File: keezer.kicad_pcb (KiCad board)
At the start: 2 copper layers, 48 parts, among them J1 Barrel_Jack, J10 REF, J11 Display, J12 Mode Switch, J13 Tare Switch, J14 Rocker Switch, J15 Conn_01x03_Male, J16 Conn_01x03_Male, J2 Relay, J3 Fan, J4 Conn_01x03_Female, J5 Conn_01x03_Female, J6 Conn_01x04_Female, J7 Conn_01x04_Female, J8 Conn_01x04_Female, J9 Conn_01x04_Female, Q1 2N5194, U1 4N25, U2 INA828, U3 INA828, U4 INA828, U5 INA828

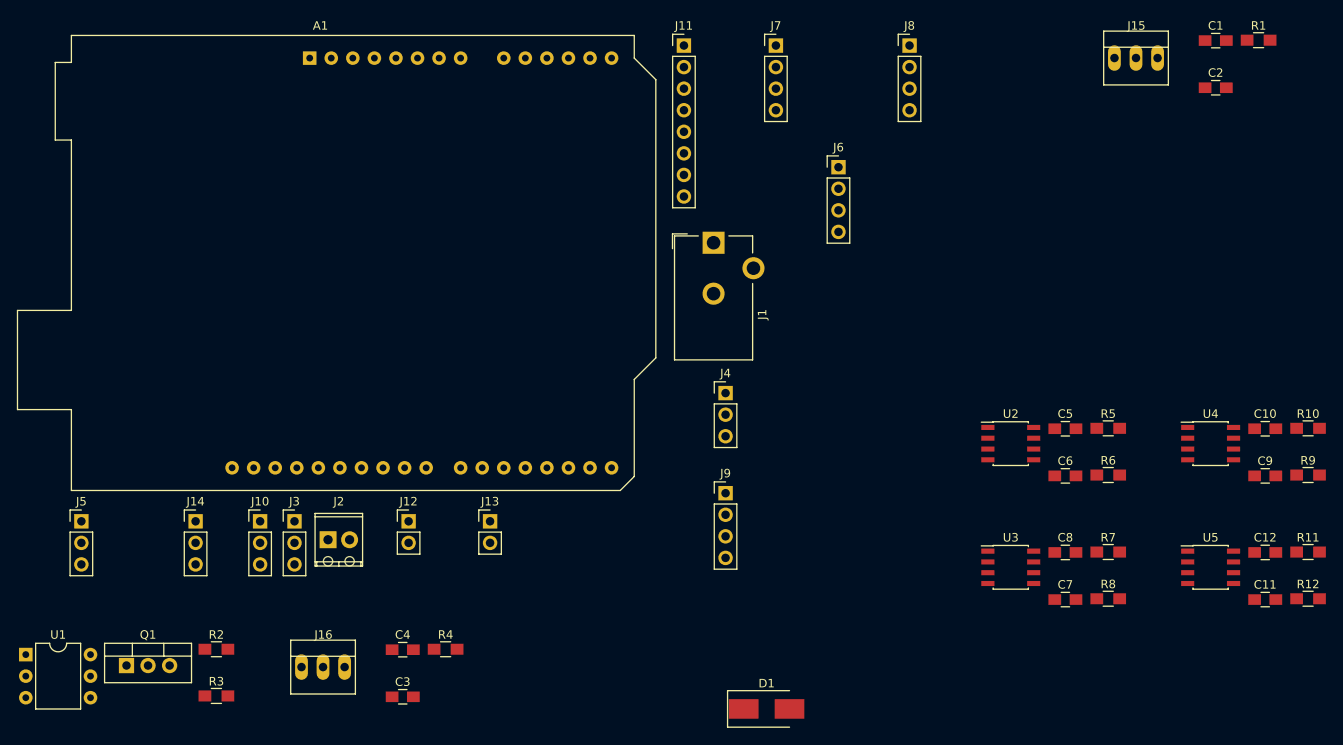
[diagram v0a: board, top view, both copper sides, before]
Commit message: Pretty much ready to go. Should verify barrel jack first. Needs a logo.
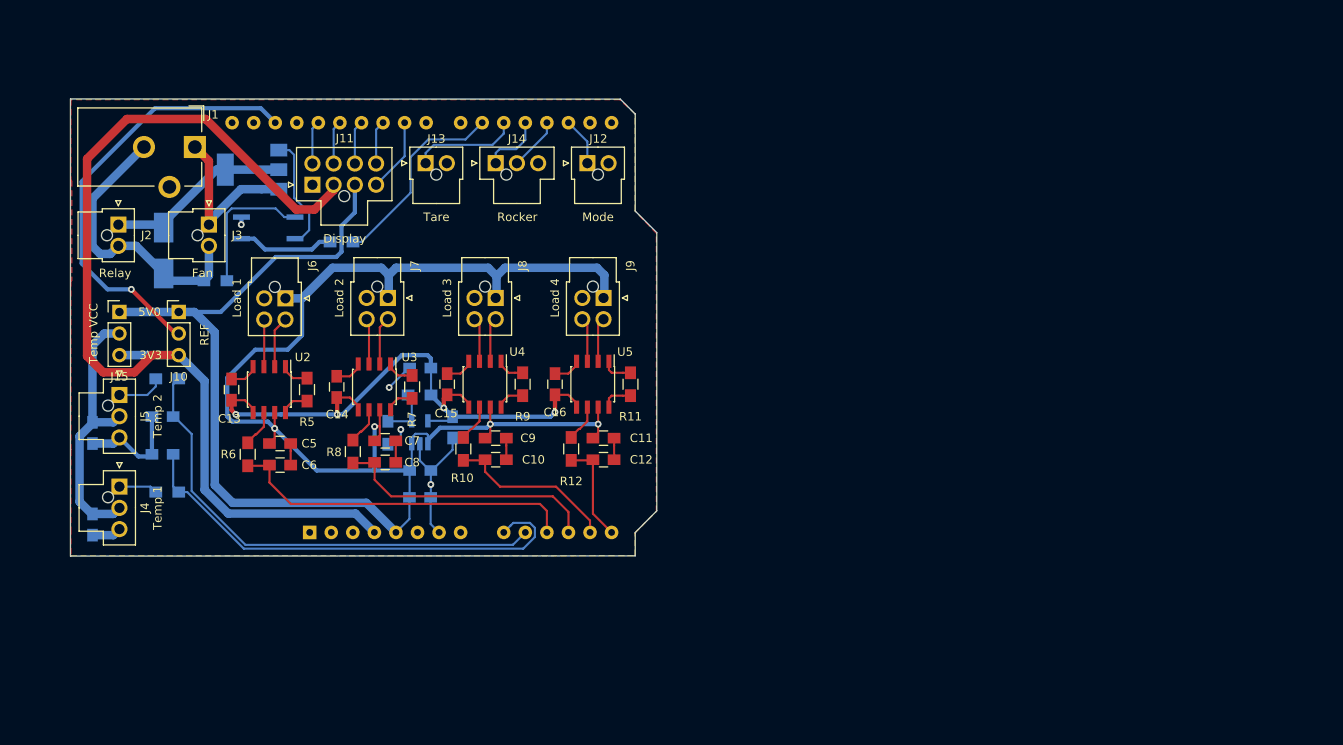
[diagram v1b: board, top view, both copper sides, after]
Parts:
- removed J16: Conn_01x03_Male, Connectors:PINHEAD1-3
- added C13: 1uF, Capacitors_SMD:C_0805_HandSoldering, F.Cu at (100.3, 92.1)
- added C14: 1uF, Capacitors_SMD:C_0805_HandSoldering, F.Cu at (112.7, 91.8)
- added C15: 1uF, Capacitors_SMD:C_0805_HandSoldering, F.Cu at (125.7, 91.4)
- added C16: 1uF, Capacitors_SMD:C_0805_HandSoldering, F.Cu at (138.4, 91.4)
- added C17: 10uF, Capacitors_SMD:C_0805_HandSoldering, B.Cu at (122.5, 104.8)
- added C18: 0.1uF, Capacitors_SMD:C_0805_HandSoldering, B.Cu at (122.6, 101.6)
- added C19: 0.1uF, Capacitors_SMD:C_0805_HandSoldering, B.Cu at (126.4, 96.5)
- added C20: 10uF, Capacitors_SMD:C_0805_HandSoldering, B.Cu at (122.6, 89.5)
- added R13: DNP, Resistors_SMD:R_0805_HandSoldering, B.Cu at (122.5, 92.7)
- added R14: DNP, Resistors_SMD:R_0805_HandSoldering, B.Cu at (118.7, 97.2)
- added U6: LDK320M18R, TO_SOT_Packages_SMD:SOT-23-5_HandSoldering, B.Cu at (122.5, 97.1)
- A1, C1, C2, C3, C4, D1, R1, R2, R3, R4: moved to B.Cu
- J11: footprint Pin_Headers:Pin_Header_Straight_1x08_Pitch2.54mm -> Connectors_Molex:Molex_NanoFit_2x04x2.50mm_Straight
- J12: value Mode Switch -> Mode; footprint Pin_Headers:Pin_Header_Straight_1x02_Pitch2.54mm -> Connectors_Molex:Molex_NanoFit_1x02x2.50mm_Straight
- J13: value Tare Switch -> Tare; footprint Pin_Headers:Pin_Header_Straight_1x02_Pitch2.54mm -> Connectors_Molex:Molex_NanoFit_1x02x2.50mm_Straight
- J14: value Rocker Switch -> Rocker; footprint Pin_Headers:Pin_Header_Straight_1x03_Pitch2.54mm -> Connectors_Molex:Molex_NanoFit_1x03x2.50mm_Straight
- J15: value Conn_01x03_Male -> Temp VCC; footprint Connectors:PINHEAD1-3 -> Pin_Headers:Pin_Header_Straight_1x03_Pitch2.54mm
- J2: footprint TerminalBlock_Phoenix:TerminalBlock_Phoenix_MPT-2.54mm_2pol -> Connectors_Molex:Molex_NanoFit_1x02x2.50mm_Straight
- J3: footprint Pin_Headers:Pin_Header_Straight_1x03_Pitch2.54mm -> Connectors_Molex:Molex_NanoFit_1x02x2.50mm_Straight
- J4: value Conn_01x03_Female -> Temp 1; footprint Pin_Headers:Pin_Header_Straight_1x03_Pitch2.54mm -> Connectors_Molex:Molex_NanoFit_1x03x2.50mm_Straight
- J5: value Conn_01x03_Female -> Temp 2; footprint Pin_Headers:Pin_Header_Straight_1x03_Pitch2.54mm -> Connectors_Molex:Molex_NanoFit_1x03x2.50mm_Straight
- J6: value Conn_01x04_Female -> Load 1; footprint Pin_Headers:Pin_Header_Straight_1x04_Pitch2.54mm -> Connectors_Molex:Molex_NanoFit_2x02x2.50mm_Straight
- J7: value Conn_01x04_Female -> Load 2; footprint Pin_Headers:Pin_Header_Straight_1x04_Pitch2.54mm -> Connectors_Molex:Molex_NanoFit_2x02x2.50mm_Straight
- J8: value Conn_01x04_Female -> Load 3; footprint Pin_Headers:Pin_Header_Straight_1x04_Pitch2.54mm -> Connectors_Molex:Molex_NanoFit_2x02x2.50mm_Straight
- J9: value Conn_01x04_Female -> Load 4; footprint Pin_Headers:Pin_Header_Straight_1x04_Pitch2.54mm -> Connectors_Molex:Molex_NanoFit_2x02x2.50mm_Straight
- Q1: value 2N5194 -> BCP51; footprint TO_SOT_Packages_THT:TO-220-3_Vertical -> TO_SOT_Packages_SMD:SOT-223-3_TabPin2; moved to B.Cu
- R11, R5, R7, R9: value 49.9 -> 75.0
- U1: value 4N25 -> FOD817D3SD; footprint Housings_DIP:DIP-6_W7.62mm -> Housings_SOIC:SO-4_4.4x3.6mm_Pitch2.54mm; moved to B.Cu
- moved C1 140.1 mm to (83.9, 97.2), turned to 270 degrees
- moved R1 134.6 mm to (92.8, 90.8), turned to 180 degrees
- moved C2 130.0 mm to (92.2, 95.2), turned to 180 degrees
- moved J15 121.0 mm to (87.1, 82.9)
- moved R6 101.4 mm to (102.2, 99.7), turned to 90 degrees
- moved R10 99.5 mm to (127.6, 99.1), turned to 90 degrees
- moved R5 94.5 mm to (109.2, 92.1), turned to 270 degrees
- moved R9 93.1 mm to (134.6, 91.4), turned to 270 degrees
- moved C5 92.5 mm to (106.0, 98.4)
- moved C6 92.5 mm to (106.0, 101.0)
- moved C9 90.7 mm to (131.4, 97.8)
- moved C10 90.7 mm to (131.4, 100.3)
- moved R8 90.6 mm to (114.6, 99.4), turned to 90 degrees
- moved D1 89.2 mm to (92.3, 75.7), turned to 270 degrees
- moved R12 88.6 mm to (140.3, 99.1), turned to 90 degrees
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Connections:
- A1 pad 20: Net-(A1-Pad18) -> Net-(A1-Pad20)
- C3 pad 1: /sheet5A46696F/Power -> /Temp Sensor Interface 2/Power
- J11 pad 4: Net-(A1-Pad27) -> Net-(A1-Pad24)
- J11 pad 6: Net-(A1-Pad26) -> Net-(A1-Pad27)
- J11 pad 7: Net-(A1-Pad25) -> Net-(A1-Pad26)
- J11 pad 8: Net-(A1-Pad24) -> Net-(A1-Pad25)
- J13 pad 1: Net-(A1-Pad18) -> Net-(A1-Pad20)
- J14 pad 1: Net-(A1-Pad18) -> Net-(A1-Pad19)
- J14 pad 2: Net-(A1-Pad19) -> Net-(A1-Pad18)
- J15 pad 1: +3V3 -> +5V
- J15 pad 3: +5V -> +3V3
- J4 pad 2: /sheet5A46696F/Power -> /Temp Sensor Interface 2/Power
- J6 pad 3: /Strain Gauge Interface 1/O+ -> /Strain Gauge Interface 1/O-
- J6 pad 4: /Strain Gauge Interface 1/O- -> /Strain Gauge Interface 1/O+
- J7 pad 3: /sheet5A466294/O+ -> /sheet5A466294/O-
- J7 pad 4: /sheet5A466294/O- -> /sheet5A466294/O+
- J8 pad 3: /sheet5A4663CA/O+ -> /sheet5A4663CA/O-
- J8 pad 4: /sheet5A4663CA/O- -> /sheet5A4663CA/O+
- J9 pad 3: /sheet5A4665A5/O+ -> /sheet5A4665A5/O-
- J9 pad 4: /sheet5A4665A5/O- -> /sheet5A4665A5/O+
- Q1 pad 1: /Relay Interface/+12V_ISO -> Net-(Q1-Pad1)
- Q1 pad 2: Net-(Q1-Pad2) -> /Relay Interface/Coil+
- Q1 pad 3: /Relay Interface/Coil+ -> /Relay Interface/+12V_ISO
- U1 pad 3: Net-(U1-Pad3) -> Net-(R3-Pad1)
- U1 pad 4: Net-(R3-Pad1) -> Net-(Q1-Pad1)
- U2 pad 5: GND -> /Strain Gauge Interface 1/REF
- U3 pad 5: GND -> /Strain Gauge Interface 1/REF
- U4 pad 5: GND -> /Strain Gauge Interface 1/REF
- U5 pad 5: GND -> /Strain Gauge Interface 1/REF
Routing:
- net +5V: track 0.00 -> 233.5 mm, vias 0 -> 4
- net +3V3: track 0.00 -> 119.0 mm
- net /Strain Gauge Interface 1/REF: track 0.00 -> 71.2 mm, vias 0 -> 4
- net GND: track 0.00 -> 63.8 mm, vias 0 -> 4
- net /Temp Sensor Interface 2/Temp_Out: track 0.00 -> 57.0 mm
- net /sheet5A46696F/Temp_Out: track 0.00 -> 55.5 mm
- net Net-(A1-Pad30): track 0.00 -> 51.6 mm, vias 0 -> 1
- net /Strain Gauge Interface 1/Weight_Out: track 0.00 -> 41.2 mm
- net /Relay Interface/Coil-: track 0.00 -> 34.1 mm
- net /Temp Sensor Interface 2/Power: track 0.00 -> 31.9 mm
- net /sheet5A466294/Weight_Out: track 0.00 -> 31.5 mm
- net /Relay Interface/Relay_In: track 0.00 -> 23.5 mm
- net /Relay Interface/Coil+: track 0.00 -> 22.2 mm
- net /sheet5A4663CA/Weight_Out: track 0.00 -> 20.1 mm
- net /Relay Interface/+12V_ISO: track 0.00 -> 20.0 mm
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- added copper zone on F.Cu, net GND
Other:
- board outline added: 69.1 x 53.8 mm
- board text added: "3V3"
- board text added: "5V0"
